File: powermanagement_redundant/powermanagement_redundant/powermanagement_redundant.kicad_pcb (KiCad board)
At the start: 4 copper layers, 121 x 17.5 mm, 48 parts, among them J1 Screw_Terminal_01x01, J2 Screw_Terminal_01x01, J3 Screw_Terminal_01x01, J4 Screw_Terminal_01x01, J5 Screw_Terminal_01x01, J6 Screw_Terminal_01x01, J7 Screw_Terminal_01x01, J8 Screw_Terminal_01x01, SW1 SW_DIP_x01, SW2 SW_DIP_x01

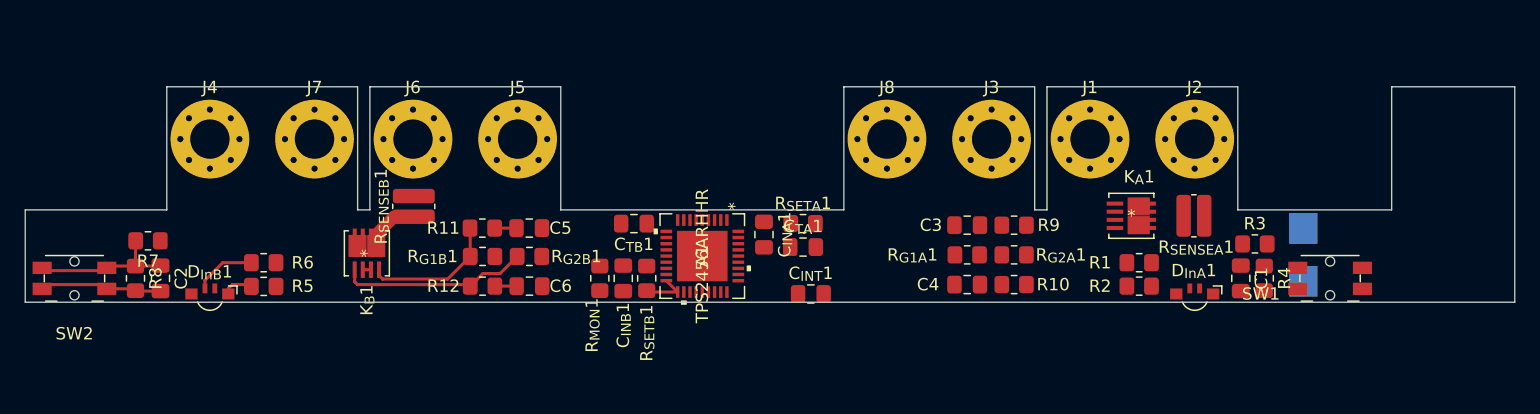
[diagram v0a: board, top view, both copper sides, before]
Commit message: add PCB and make it for Aisler work
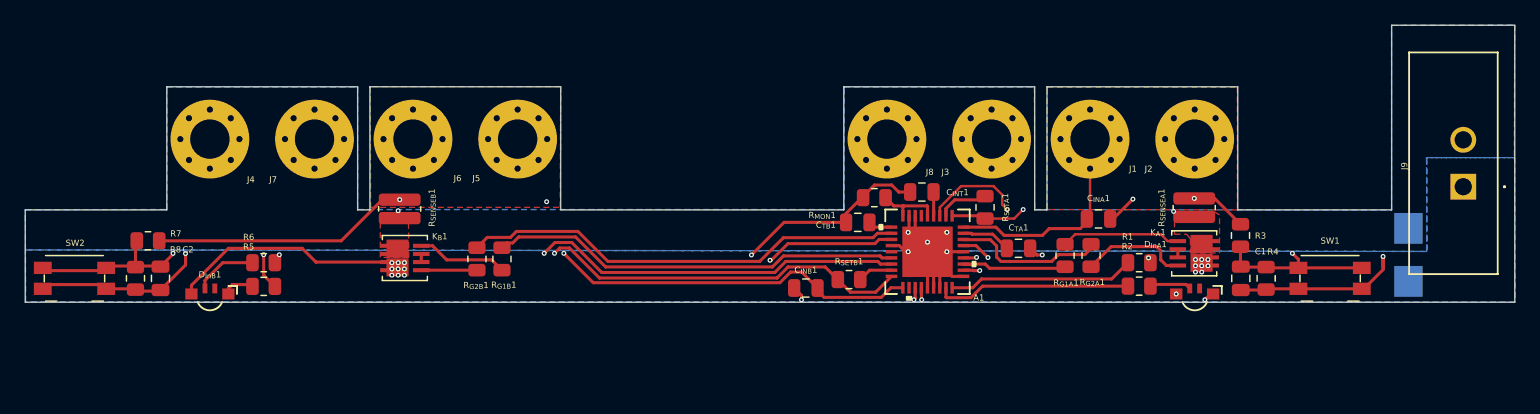
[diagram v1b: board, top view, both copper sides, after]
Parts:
- removed C3, C4, C5, C6: 10n, Capacitor_SMD:C_0805_2012Metric_Pad1.18x1.45mm_HandSolder
- removed R10, R11, R12, R9: 1k, Resistor_SMD:R_0805_2012Metric_Pad1.20x1.40mm_HandSolder
- added J9: 691323300002, KiCad:691323300002, F.Cu at (136.8, 28.1)
- C1, C2, C_{INA}1, C_{INB}1, C_{INT}1, C_{TA}1, C_{TB}1: footprint Capacitor_SMD:C_0805_2012Metric_Pad1.18x1.45mm_HandSolder -> Capacitor_SMD:C_0805_2012Metric
- R1, R2, R3, R4, R5, R6, R7, R8, R_{G1A}1, R_{G1B}1, R_{G2A}1, R_{G2B}1, R_{MON}1, R_{SETA}1, R_{SETB}1: footprint Resistor_SMD:R_0805_2012Metric_Pad1.20x1.40mm_HandSolder -> Resistor_SMD:R_0805_2012Metric
- R_{SENSEA}1, R_{SENSEB}1: footprint Resistor_SMD:R_0612_1632Metric_Pad1.18x3.40mm_HandSolder -> Resistor_SMD:R_0612_1632Metric
- SW1, SW2: footprint Button_Switch_SMD:Panasonic_EVQPUL_EVQPUC -> Button_Switch_SMD:Panasonic_EVQPUK_EVQPUB
- moved C_{INA}1 27.2 mm to (107.2, 30.7), turned to 0 degrees
- moved R_{MON}1 23.2 mm to (89.0, 29.0), turned to 180 degrees
- moved A1 18.3 mm to (93.3, 33.4)
- moved C_{TB}1 18.2 mm to (87.6, 31.0)
- moved C_{TA}1 17.5 mm to (100.7, 33.1)
- moved R_{SETB}1 16.4 mm to (86.9, 35.7), turned to 180 degrees
- moved C_{INB}1 14.9 mm to (83.4, 36.3), turned to 180 degrees
- moved R_{SETA}1 14.8 mm to (98.0, 29.8), turned to -90 degrees
- moved C_{INT}1 12.2 mm to (92.8, 28.5), turned to 180 degrees
- moved D1 8.53 mm to (132.4, 33.7), turned to 90 degrees
- moved R_{G1A}1 7.95 mm to (104.5, 33.7), turned to 90 degrees
- moved R_{G2A}1 6.25 mm to (106.6, 33.7), turned to -90 degrees
- moved K_{A}1 5.95 mm to (115.0, 33.5)
- moved R_{G2B}1 4.27 mm to (56.7, 34.0), turned to -90 degrees
- moved K_{B}1 3.11 mm to (50.8, 33.9), turned to 180 degrees
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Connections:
- net SETBB renamed SETB
- A1 pad 9: MONB -> MONA
- R_{MON}1 pad 1: SETA -> MONA
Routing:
- net INB: track 3.87 -> 102.0 mm, vias 0 -> 4
- net ENB: track 11.9 -> 82.4 mm, vias 0 -> 2
- net GND: track 10.0 -> 76.3 mm, vias 0 -> 11
- net FLTB: track 0.00 -> 58.3 mm, vias 0 -> 2
- net PGB: track 0.00 -> 55.5 mm, vias 0 -> 2
- net SENMB: track 4.16 -> 45.4 mm, vias 0 -> 2
- net INA: track 0.00 -> 41.1 mm, vias 0 -> 2
- net ENA: track 0.00 -> 40.7 mm, vias 0 -> 2
- net GAT2B: track 0.00 -> 36.2 mm
- net LOAD: track 0.00 -> 35.5 mm, vias 0 -> 20
- net GAT1B: track 0.00 -> 33.5 mm
- net SENMA: track 0.00 -> 24.4 mm, vias 0 -> 2
- net PGA: track 0.00 -> 16.0 mm
- net FLTA: track 0.00 -> 15.1 mm
- net GAT2A: track 0.00 -> 12.1 mm
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- added copper zone on B.Cu, net GND
- added copper zone on In2.Cu, net GND
- added copper zone on F.Cu, net INA
- added copper zone on F.Cu, net INB
- added copper zone on B.Cu, net LOAD
- added copper zone on In2.Cu, net LOAD
- added copper zone on F.Cu, net SENMA
- added copper zone on F.Cu, net SENMB
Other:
- board size 121 x 17.5 mm -> 121 x 22.5 mm

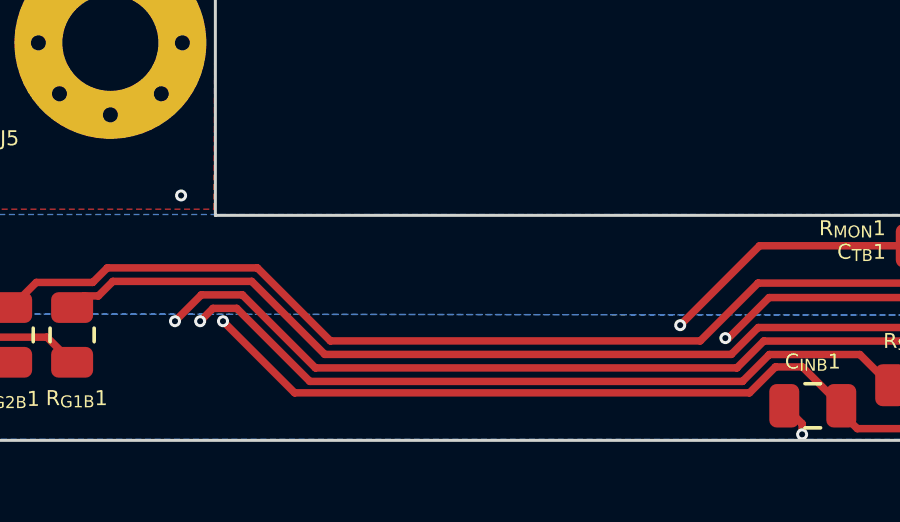
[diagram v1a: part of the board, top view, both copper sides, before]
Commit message: add text
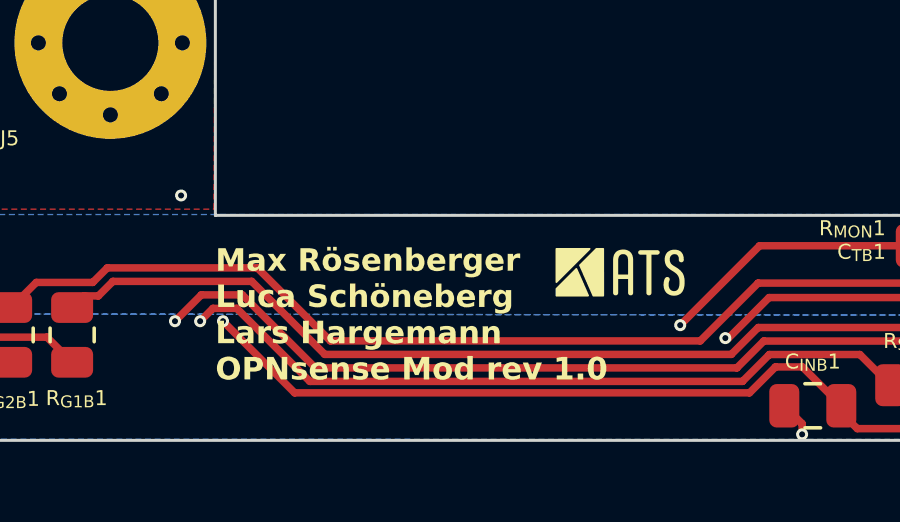
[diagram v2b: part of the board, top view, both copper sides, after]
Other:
- board text added: "Max Rösenberger Luca Schöneberg Lars Hargemann OPNsense Mod rev 1.0"

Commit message: update some text
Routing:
- net LOAD: vias 20 -> 21
- added copper zone on F.Cu, net LOAD
- removed copper zone on In2.Cu, net LOAD
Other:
- board text added: "2023"
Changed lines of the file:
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@@
   (gr_line (start 47 30) (end 48 30)
     (stroke (width 0.1) (type solid)) (layer "Edge.Cuts"))
+  (gr_text "2023" (at 20.066 31.115) (layer "F.SilkS")
+    (effects (font (size 0.75 0.75) (thickness 0.1875) bold) (justify left bottom))
+  )
   (gr_text "Max Rösenberger\nLuca Schöneberg\nLars Hargemann\nOPNsense Mod rev 1.0" (at 63.5 35.56) (layer "F.SilkS")
     (effects (font (size 0.75 0.75) (thickness 0.1875) bold) (justify left bottom))
@@
   (via (at 116.078 34.036) (size 0.4) (drill 0.2) (layers "F.Cu" "B.Cu") (net 9))
   (via (at 50.292 34.29) (size 0.4) (drill 0.2) (layers "F.Cu" "B.Cu") (net 9))
+  (via (at 116.078 35.052) (size 0.4) (drill 0.2) (layers "F.Cu" "B.Cu") (free) (net 9))
   (via (at 113.5 36.83) (size 0.4) (drill 0.2) (layers "F.Cu" "B.Cu") (net 9))
   (via (at 115.062 35.052) (size 0.4) (drill 0.2) (layers "F.Cu" "B.Cu") (net 9))
@@
     )
   )
+  (zone (net 9) (net_name "LOAD") (layer "F.Cu") (hatch edge 0.5)
+    (priority 4)
+    (connect_pads yes (clearance 0))
+    (min_thickness 0.25) (filled_areas_thickness no)
+    (fill yes (thermal_gap 0.5) (thermal_bridge_width 0.5))
+    (polygon
+      (pts
+        (xy 114.7318 33.5788)
+        (xy 116.9924 33.5788)
+        (xy 116.9924 35.4076)
+        (xy 116.3066 35.4076)
+        (xy 115.9002 35.4076)
+        (xy 114.7318 35.4076)
+      )
+    )
+  )
   (zone (net 6) (net_name "GND") (layer "In2.Cu") (hatch edge 0.5)
     (connect_pads no (clearance 0.508))
@@
       )
     )
-  )
-  (zone (net 9) (net_name "LOAD") (layer "In2.Cu") (hatch edge 0.5)
-    (priority 4)
-    (connect_pads yes (clearance 0))
-    (min_thickness 0.25) (filled_areas_thickness no)
-    (fill yes (thermal_gap 0.5) (thermal_bridge_width 0.5))
-    (polygon
-      (pts
-        (xy 114.7318 33.5788)
-        (xy 117.7036 33.5788)
-        (xy 117.7036 36.0426)
-        (xy 115.9256 36.0426)
-        (xy 115.9256 35.6616)
-        (xy 114.7318 35.6616)
-      )
-    )

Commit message: rev.01
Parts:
- moved C2 5.64 mm to (36.6, 35.5)
- moved D_{InB}1 5.64 mm to (40.6, 36.7)
- moved R6 5.64 mm to (45.0, 34.2)
- moved R8 5.64 mm to (34.6, 35.5)
- moved SW2 5.64 mm to (29.6, 35.5)
- moved R7 5.64 mm to (35.6, 32.4)
- moved R5 5.64 mm to (45.0, 36.2)
- moved R2 0.08 mm to (110.5, 36.3)
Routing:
- net PGB: track 55.5 -> 49.7 mm
- net FLTB: track 58.3 -> 53.0 mm
- net ENB: track 82.4 -> 78.0 mm
- net INB: track 102.0 -> 97.8 mm
- net LOAD: track 35.5 -> 32.4 mm, vias 21 -> 22
- net PGA: track 16.0 -> 16.6 mm
- net SENMB: track 45.4 -> 46.1 mm
- net INA: track 41.1 -> 41.8 mm
- net Net-(D_{InA}1-R): track 7.05 -> 6.61 mm, vias 2 -> 0
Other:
- board size 121 x 22.5 mm -> 115.2 x 22.5 mm

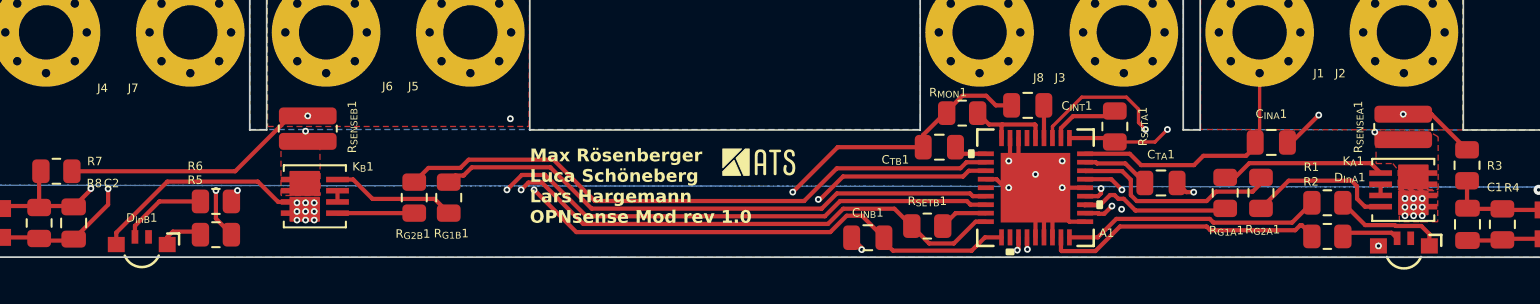
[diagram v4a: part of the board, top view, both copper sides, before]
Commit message: upgrade mosfet footprint, change some values
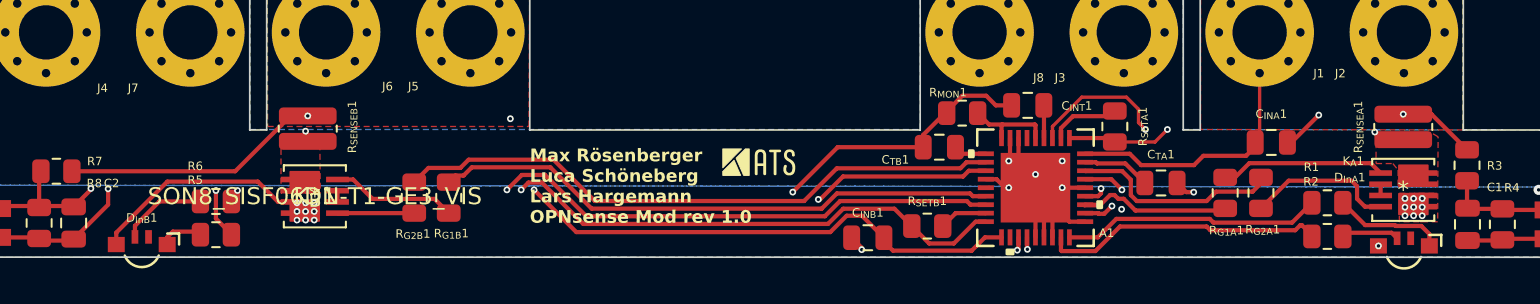
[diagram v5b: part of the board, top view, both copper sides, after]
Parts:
- C1: value 22nF -> 47nf
- C2: value 22nf -> 47nf
- C_{TA}1, C_{TB}1: value 33n -> 47n
- K_{A}1, K_{B}1: value SISF00DN-T1-GE3 -> SON8_SISF06DN-T1-GE3_VIS
- R3, R7: value 249k -> 330k
- R4, R8: value 51k -> 68k
- R_{MON}1: value 4,7k -> 6,8k
- R_{SETA}1, R_{SETB}1: value 510 1% -> 680 1%

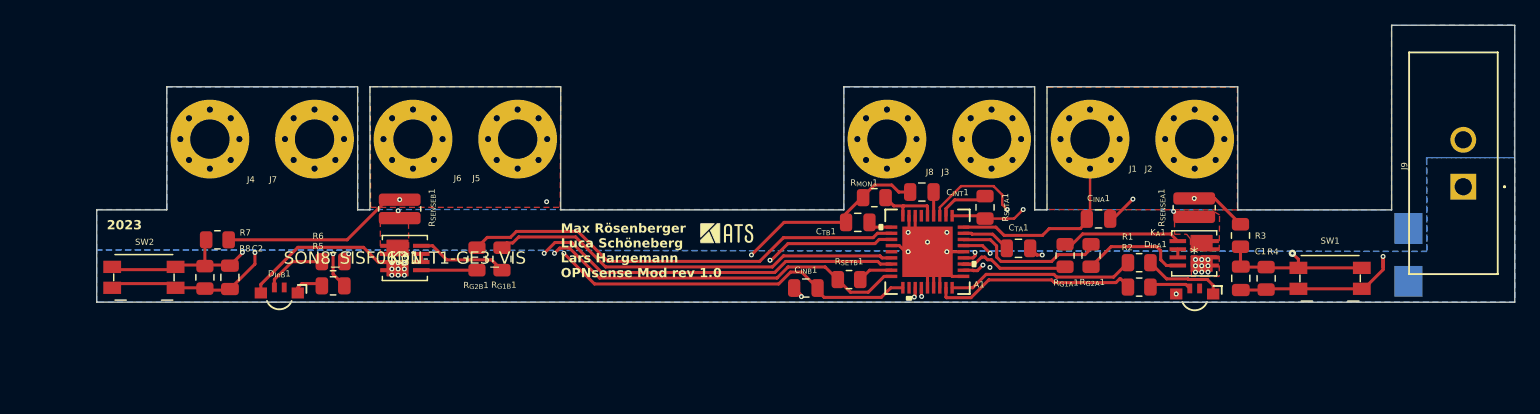
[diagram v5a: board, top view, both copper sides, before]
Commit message: Mosfets getauscht.
Die Mosfets hab ich gegen CSD87313DMS getauscht. Im gleichen Schritt hab ich die Pads überarbeitet. Die haben jetzt einen vollständigen Übergangauf zum Backlayer.
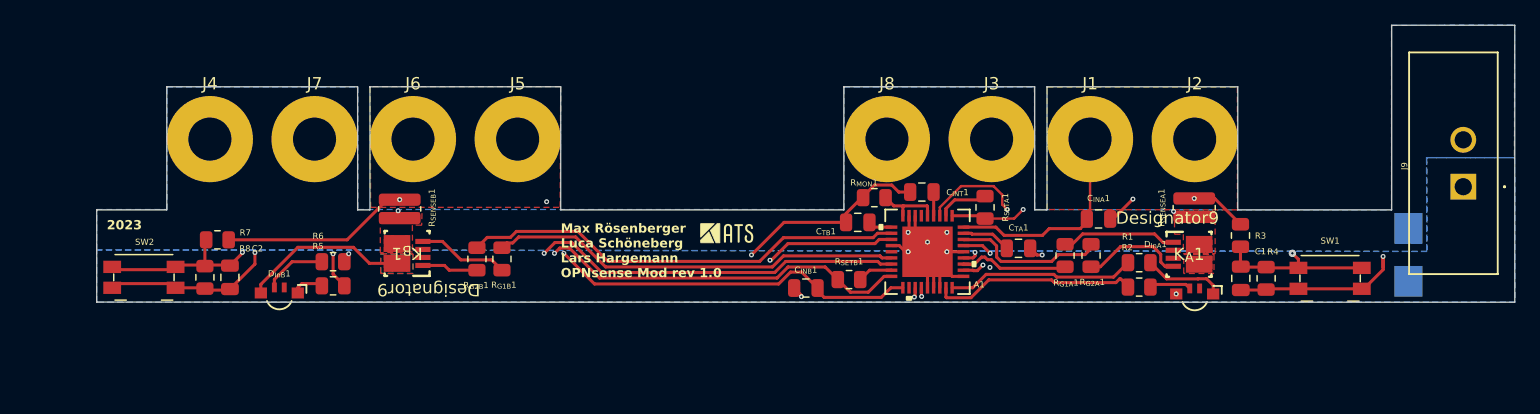
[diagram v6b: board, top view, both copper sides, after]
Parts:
- J1, J2, J3, J4, J5, J6, J7, J8: footprint MountingHole:MountingHole_3.2mm_M3_Pad_Via -> MountingHole:MountingHole_3.5mm_Pad
- K_{A}1, K_{B}1: value SON8_SISF06DN-T1-GE3_VIS -> CSD87313DMS; footprint SISF00DN-1:SISF00DN-T1-GE3 -> CSD87313DMS:DMS0008A
- moved K_{A}1 0.43 mm to (114.5, 33.6)
- moved K_{B}1 0.41 mm to (51.0, 33.5)
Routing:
- net LOAD: track 32.4 -> 27.7 mm, vias 22 -> 4
- net SENMB: track 46.1 -> 45.4 mm
- net Net-(K_{B}1-D-Pad2): track 0.66 -> 0.00 mm
- net Net-(K_{A}1-D-Pad2): track 0.66 -> 0.00 mm
- added copper zone on In1.Cu, net LOAD
- added copper zone on In2.Cu, net LOAD

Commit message: Kompletto auf anderes ic umgebaut
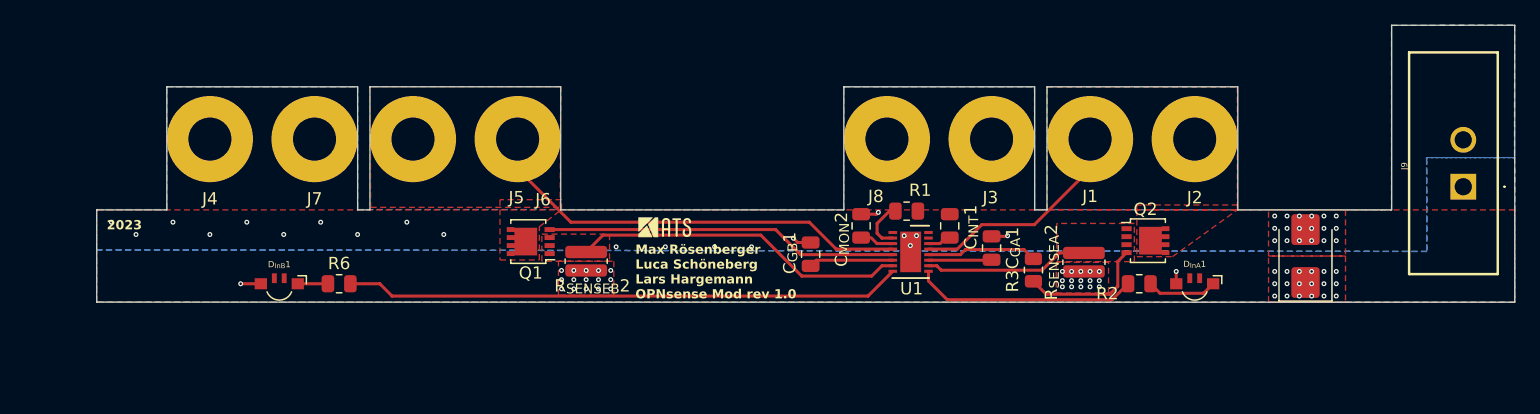
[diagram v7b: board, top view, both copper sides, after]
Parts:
- removed A1: TPS2456ARHHR, TPS2456:TPS2456ARHHR
- removed C1, C2: 47nf, Capacitor_SMD:C_0805_2012Metric
- removed C_{INA}1, C_{INB}1: 100n, Capacitor_SMD:C_0805_2012Metric
- removed C_{TA}1, C_{TB}1: 47n, Capacitor_SMD:C_0805_2012Metric
- removed K_{A}1, K_{B}1: CSD87313DMS, CSD87313DMS:DMS0008A
- removed R4, R8: 68k, Resistor_SMD:R_0805_2012Metric
- removed R5, R_{MON}1: 6,8k, Resistor_SMD:R_0805_2012Metric
- removed R7: 330k, Resistor_SMD:R_0805_2012Metric
- removed R_{G1A}1, R_{G1B}1, R_{G2A}1, R_{G2B}1: 10, Resistor_SMD:R_0805_2012Metric
- removed R_{SENSEA}1, R_{SENSEB}1: 5m 1% 2W, Resistor_SMD:R_0612_1632Metric
- removed R_{SETA}1, R_{SETB}1: 680 1%, Resistor_SMD:R_0805_2012Metric
- removed SW1, SW2: SW_DIP_x01, Button_Switch_SMD:Panasonic_EVQPUK_EVQPUB
- added C_{GA}1: 47n, Capacitor_SMD:C_0805_2012Metric, F.Cu at (98.5, 33.1)
- added C_{GB}1: 47n, Capacitor_SMD:C_0805_2012Metric, F.Cu at (83.8, 33.6)
- added C_{MON}2: 47n, Capacitor_SMD:C_0805_2012Metric, F.Cu at (87.9, 31.3)
- added Q1: BUK9M11-40EX, Package_TO_SOT_SMD:LFPAK33, F.Cu at (61.1, 32.6)
- added Q2: BUK9M11-40EX, Package_TO_SOT_SMD:LFPAK33, F.Cu at (111.0, 32.5)
- added R_{SENSEA}2: 2m 1% 2W, Resistor_SMD:R_0612_1632Metric, F.Cu at (106.0, 34.2)
- added R_{SENSEB}2: 2m 1% 2W, Resistor_SMD:R_0612_1632Metric, F.Cu at (65.6, 34.2)
- added U1: LTC4370xDE, Package_DFN_QFN:DFN-16-1EP_3x4mm_P0.45mm_EP1.7x3.3mm, F.Cu at (91.9, 33.4)
- D1: moved to F.Cu
- R1: value 6,8k -> 27k
- R2, R6: value 5,1k -> 6k8
- R3: value 330k -> 0
- moved R1 19.3 mm to (91.6, 30.1), turned to 0 degrees
- moved R3 17.1 mm to (101.9, 34.9)
- moved D1 8.36 mm to (124.0, 33.8)
- moved C_{INT}1 3.56 mm to (95.1, 31.3), turned to 90 degrees
- moved R6 1.86 mm to (45.5, 36.0)
- moved D_{InA}1 0.83 mm to (115.0, 36.0)
- moved D_{InB}1 0.75 mm to (40.6, 36.0)
- moved R2 0.27 mm to (110.5, 36.0)
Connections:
- D_{InA}1 pad 3: Net-(D_{InA}1-G) -> unconnected-(D_{InA}1-G-Pad3)
- D_{InB}1 pad 3: Net-(D_{InB}1-G) -> unconnected-(D_{InB}1-G-Pad3)
- R1 pad 1: Net-(D_{InA}1-R) -> RANGE
- R1 pad 2: FLTA -> GND
- R2 pad 1: Net-(D_{InA}1-G) -> Net-(D_{InA}1-R)
- R3 pad 1: INA -> GTA
- R3 pad 2: ENA -> Net-(Q2-G)
- R6 pad 1: Net-(D_{InB}1-G) -> Net-(D_{InB}1-R)
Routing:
- net ENB: track 78.0 -> 0.00 mm, vias 2 -> 0
- net GND: track 76.0 -> 7.92 mm, vias 11 -> 38
- net INB: track 97.8 -> 35.6 mm, vias 4 -> 0
- net FLTB: track 53.0 -> 0.00 mm, vias 2 -> 0
- net SENMB: track 45.4 -> 0.00 mm, vias 2 -> 0
- net ENA: track 40.5 -> 0.00 mm, vias 2 -> 0
- net GAT2B: track 36.2 -> 0.00 mm
- net GAT1B: track 33.5 -> 0.00 mm
- net GTB: track 0.00 -> 28.7 mm
- net SENB: track 0.00 -> 27.2 mm
- net LOAD: track 27.7 -> 2.64 mm, vias 4 -> 50
- net SENMA: track 24.4 -> 0.00 mm, vias 2 -> 0
- net INA: track 41.8 -> 18.2 mm, vias 2 -> 0
- net FLTA: track 15.3 -> 0.00 mm
- net SENA: track 0.00 -> 15.1 mm
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- added copper zone on F.Cu, net GND
- added copper zone on F.Cu, net SENA
- added copper zone on F.Cu, net SENB
- removed copper zone on In2.Cu, net GND
- removed copper zone on In1.Cu, net LOAD
- removed copper zone on In2.Cu, net LOAD
- removed copper zone on F.Cu, net SENMA
- removed copper zone on F.Cu, net SENMB
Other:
- copper layers 4 -> 2
